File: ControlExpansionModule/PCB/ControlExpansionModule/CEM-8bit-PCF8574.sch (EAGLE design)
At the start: 0 parts

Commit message: Added component in the circuit
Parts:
- added C1, C2: (no value), rcl:C-EUC0805K
- added R1, R2, R3: (no value), rcl:R-EU_M1406
- added U1: PCF8574AT/3,512, PCF8574:PCF8574AT/3,512
- added X1: 43160-1204, con-molex:43160-1204
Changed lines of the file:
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@@
 <parts>
 <part name="FRAME1" library="frames" deviceset="A4L-LOC" device=""/>
+<part name="U1" library="PCF8574" deviceset="PCF8574AT/3,512" device=""/>
+<part name="R1" library="rcl" deviceset="R-EU_" device="M1406"/>
+<part name="R2" library="rcl" deviceset="R-EU_" device="M1406"/>
+<part name="R3" library="rcl" deviceset="R-EU_" device="M1406"/>
+<part name="X1" library="con-molex" deviceset="43160-*04" device="" technology="12"/>
+<part name="GND1" library="supply1" deviceset="GND" device=""/>
+<part name="P+1" library="supply1" deviceset="VCC" device=""/>
+<part name="C1" library="rcl" deviceset="C-EU" device="C0805K"/>
+<part name="C2" library="rcl" deviceset="C-EU" device="C0805K"/>
 </parts>
 <sheets>
@@
 <instances>
 <instance part="FRAME1" gate="G$1" x="0" y="0"/>
+<instance part="U1" gate="A" x="121.92" y="106.68"/>
+<instance part="R1" gate="G$1" x="71.12" y="121.92"/>
+<instance part="R2" gate="G$1" x="71.12" y="114.3"/>
+<instance part="R3" gate="G$1" x="71.12" y="106.68"/>
+<instance part="X1" gate="-1" x="25.4" y="119.38" rot="R180"/>
+<instance part="X1" gate="-2" x="25.4" y="121.92" rot="R180"/>
+<instance part="X1" gate="-3" x="25.4" y="124.46" rot="R180"/>
+<instance part="X1" gate="-4" x="25.4" y="127" rot="R180"/>
+<instance part="GND1" gate="1" x="33.02" y="109.22"/>
+<instance part="P+1" gate="VCC" x="35.56" y="139.7"/>
+<instance part="C1" gate="G$1" x="48.26" y="93.98"/>
+<instance part="C2" gate="G$1" x="48.26" y="76.2"/>
 </instances>
 <busses>

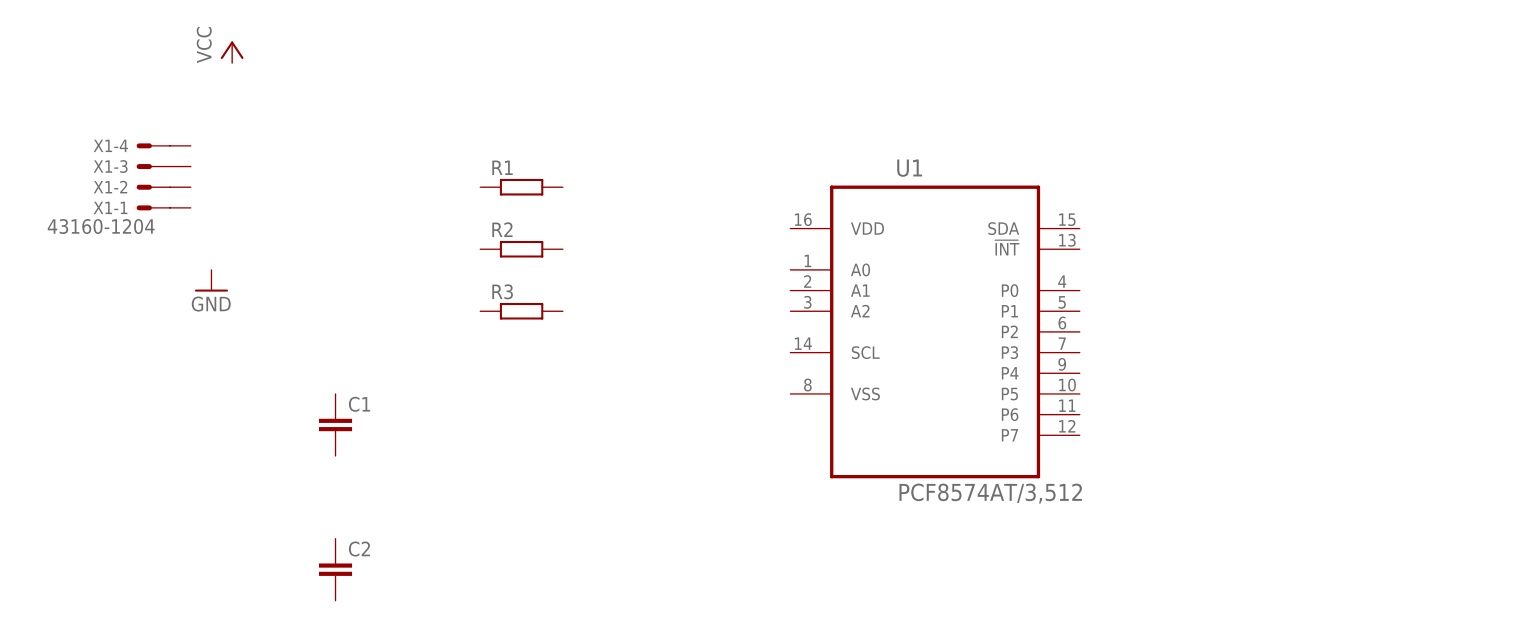
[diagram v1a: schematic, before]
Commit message: Wiring components in the Port expander circuit based on PCF8574
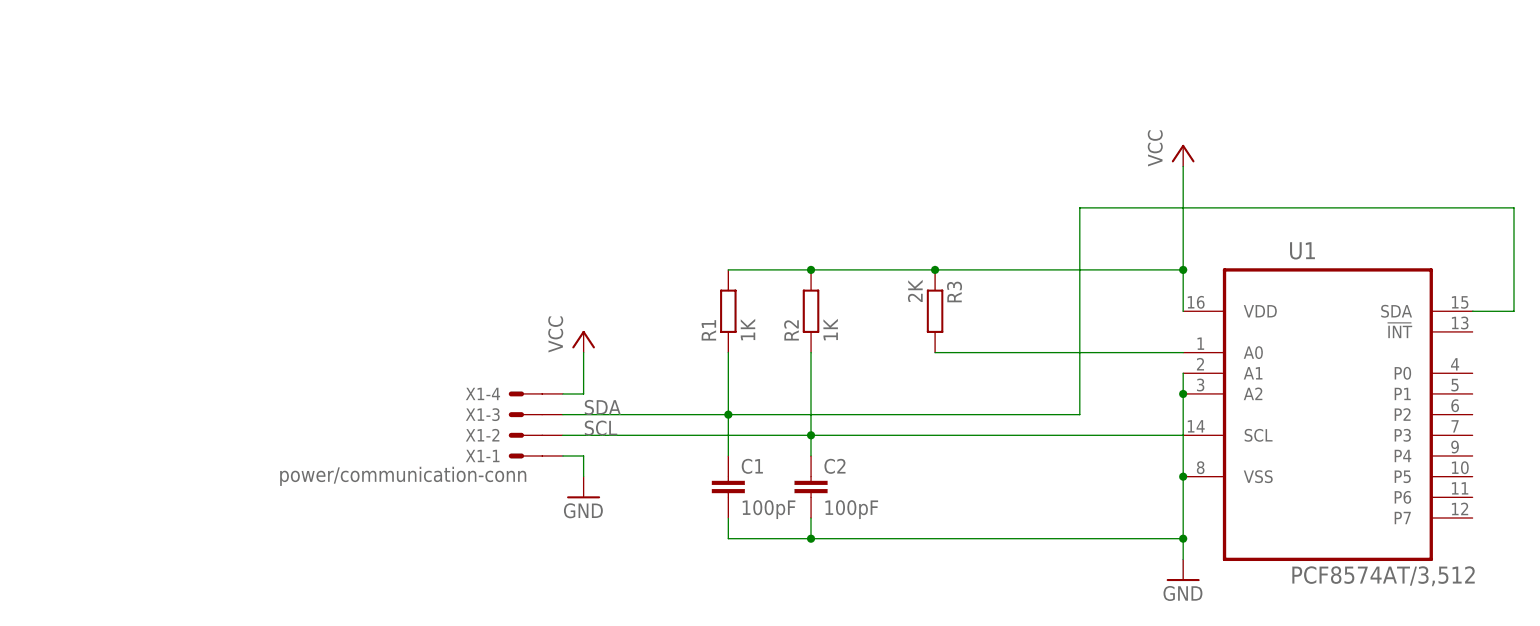
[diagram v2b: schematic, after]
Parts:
- C1, C2: value (none) -> 100pF
- R1, R2: value (none) -> 1K
- R3: value (none) -> 2K
- X1: value 43160-1204 -> power/communication-conn
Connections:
- new net GND: C1.2, C2.2, U1.A1, U1.A2, U1.VSS, X1-1.S@1
- new net N$1: R3.2, U1.A0
- new net SCL: C2.1, R2.1, U1.SCL, X1-2.S@1
- new net SDA: C1.1, R1.1, U1.SDA, X1-3.S@1
- new net VCC: R1.2, R2.2, R3.1, U1.VDD, X1-4.S@1
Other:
- moved on the sheet: C1, C2, R1, R2, R3, U1, X1-1, X1-2, X1-3, X1-4
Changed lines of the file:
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@@
 <part name="FRAME1" library="frames" deviceset="A4L-LOC" device=""/>
 <part name="U1" library="PCF8574" deviceset="PCF8574AT/3,512" device=""/>
-<part name="R1" library="rcl" deviceset="R-EU_" device="M1406"/>
-<part name="R2" library="rcl" deviceset="R-EU_" device="M1406"/>
-<part name="R3" library="rcl" deviceset="R-EU_" device="M1406"/>
-<part name="X1" library="con-molex" deviceset="43160-*04" device="" technology="12"/>
+<part name="R1" library="rcl" deviceset="R-EU_" device="M1406" value="1K"/>
+<part name="R2" library="rcl" deviceset="R-EU_" device="M1406" value="1K"/>
+<part name="R3" library="rcl" deviceset="R-EU_" device="M1406" value="2K"/>
+<part name="X1" library="con-molex" deviceset="43160-*04" device="" technology="12" value="power/communication-conn"/>
 <part name="GND1" library="supply1" deviceset="GND" device=""/>
 <part name="P+1" library="supply1" deviceset="VCC" device=""/>
-<part name="C1" library="rcl" deviceset="C-EU" device="C0805K"/>
-<part name="C2" library="rcl" deviceset="C-EU" device="C0805K"/>
+<part name="C1" library="rcl" deviceset="C-EU" device="C0805K" value="100pF"/>
+<part name="C2" library="rcl" deviceset="C-EU" device="C0805K" value="100pF"/>
+<part name="GND2" library="supply1" deviceset="GND" device=""/>
+<part name="P+2" library="supply1" deviceset="VCC" device=""/>
 </parts>
 <sheets>
@@
 <instances>
 <instance part="FRAME1" gate="G$1" x="0" y="0"/>
-<instance part="U1" gate="A" x="121.92" y="106.68"/>
-<instance part="R1" gate="G$1" x="71.12" y="121.92"/>
-<instance part="R2" gate="G$1" x="71.12" y="114.3"/>
-<instance part="R3" gate="G$1" x="71.12" y="106.68"/>
-<instance part="X1" gate="-1" x="25.4" y="119.38" rot="R180"/>
-<instance part="X1" gate="-2" x="25.4" y="121.92" rot="R180"/>
-<instance part="X1" gate="-3" x="25.4" y="124.46" rot="R180"/>
-<instance part="X1" gate="-4" x="25.4" y="127" rot="R180"/>
-<instance part="GND1" gate="1" x="33.02" y="109.22"/>
-<instance part="P+1" gate="VCC" x="35.56" y="139.7"/>
-<instance part="C1" gate="G$1" x="48.26" y="93.98"/>
-<instance part="C2" gate="G$1" x="48.26" y="76.2"/>
+<instance part="U1" gate="A" x="170.18" y="96.52"/>
+<instance part="R1" gate="G$1" x="96.52" y="106.68" rot="R90"/>
+<instance part="R2" gate="G$1" x="106.68" y="106.68" rot="R90"/>
+<instance part="R3" gate="G$1" x="121.92" y="106.68" rot="R270"/>
+<instance part="X1" gate="-1" x="71.12" y="88.9" rot="R180"/>
+<instance part="X1" gate="-2" x="71.12" y="91.44" rot="R180"/>
+<instance part="X1" gate="-3" x="71.12" y="93.98" rot="R180"/>
+<instance part="X1" gate="-4" x="71.12" y="96.52" rot="R180"/>
+<instance part="GND1" gate="1" x="78.74" y="83.82"/>
+<instance part="P+1" gate="VCC" x="152.4" y="127"/>
+<instance part="C1" gate="G$1" x="96.52" y="86.36"/>
+<instance part="C2" gate="G$1" x="106.68" y="86.36"/>
+<instance part="GND2" gate="1" x="152.4" y="73.66"/>
+<instance part="P+2" gate="VCC" x="78.74" y="104.14"/>
 </instances>
 <busses>
 </busses>
 <nets>
+<net name="VCC" class="0">
+<segment>
+<pinref part="P+1" gate="VCC" pin="VCC"/>
+<pinref part="U1" gate="A" pin="VDD"/>
+<wire x1="152.4" y1="124.46" x2="152.4" y2="111.76" width="0.1524" layer="91"/>
+<pinref part="R3" gate="G$1" pin="1"/>
+<wire x1="152.4" y1="111.76" x2="152.4" y2="106.68" width="0.1524" layer="91"/>
+<wire x1="121.92" y1="111.76" x2="152.4" y2="111.76" width="0.1524" layer="91"/>
+<pinref part="R1" gate="G$1" pin="2"/>
+<wire x1="96.52" y1="111.76" x2="106.68" y2="111.76" width="0.1524" layer="91"/>
+<pinref part="R2" gate="G$1" pin="2"/>
+<junction x="106.68" y="111.76"/>
+<wire x1="106.68" y1="111.76" x2="121.92" y2="111.76" width="0.1524" layer="91"/>
+<junction x="121.92" y="111.76"/>
+<junction x="152.4" y="111.76"/>
+</segment>
+<segment>
+<pinref part="X1" gate="-4" pin="S@1"/>
+<pinref part="P+2" gate="VCC" pin="VCC"/>
+<wire x1="76.2" y1="96.52" x2="78.74" y2="96.52" width="0.1524" layer="91"/>
+<wire x1="78.74" y1="96.52" x2="78.74" y2="101.6" width="0.1524" layer="91"/>
+</segment>
+</net>
+<net name="N$1" class="0">
+<segment>
+<pinref part="R3" gate="G$1" pin="2"/>
+<pinref part="U1" gate="A" pin="A0"/>
+<wire x1="121.92" y1="101.6" x2="152.4" y2="101.6" width="0.1524" layer="91"/>
+</segment>
+</net>
+<net name="SCL" class="0">
+<segment>
+<pinref part="R2" gate="G$1" pin="1"/>
+<pinref part="C2" gate="G$1" pin="1"/>
+<wire x1="106.68" y1="101.6" x2="106.68" y2="91.44" width="0.1524" layer="91"/>
+<pinref part="U1" gate="A" pin="SCL"/>
+<wire x1="106.68" y1="91.44" x2="106.68" y2="88.9" width="0.1524" layer="91"/>
+<wire x1="152.4" y1="91.44" x2="106.68" y2="91.44" width="0.1524" layer="91"/>
+<junction x="106.68" y="91.44"/>
+<wire x1="106.68" y1="91.44" x2="76.2" y2="91.44" width="0.1524" layer="91"/>
+<pinref part="X1" gate="-2" pin="S@1"/>
+<label x="78.74" y="91.44" size="1.778" layer="95"/>
+</segment>
+</net>
+<net name="SDA" class="0">
+<segment>
+<pinref part="R1" gate="G$1" pin="1"/>
+<pinref part="C1" gate="G$1" pin="1"/>
+<wire x1="96.52" y1="101.6" x2="96.52" y2="93.98" width="0.1524" layer="91"/>
+<pinref part="U1" gate="A" pin="SDA"/>
+<wire x1="96.52" y1="93.98" x2="96.52" y2="88.9" width="0.1524" layer="91"/>
+<wire x1="187.96" y1="106.68" x2="193.04" y2="106.68" width="0.1524" layer="91"/>
+<wire x1="193.04" y1="106.68" x2="193.04" y2="119.38" width="0.1524" layer="91"/>
+<wire x1="193.04" y1="119.38" x2="139.7" y2="119.38" width="0.1524" layer="91"/>
+<wire x1="139.7" y1="119.38" x2="139.7" y2="93.98" width="0.1524" layer="91"/>
+<wire x1="139.7" y1="93.98" x2="96.52" y2="93.98" width="0.1524" layer="91"/>
+<junction x="96.52" y="93.98"/>
+<wire x1="96.52" y1="93.98" x2="76.2" y2="93.98" width="0.1524" layer="91"/>
+<pinref part="X1" gate="-3" pin="S@1"/>
+<label x="78.74" y="93.98" size="1.778" layer="95"/>
+</segment>
+</net>
+<net name="GND" class="0">
+<segment>
+<pinref part="U1" gate="A" pin="VSS"/>
+<pinref part="GND2" gate="1" pin="GND"/>
+<wire x1="152.4" y1="86.36" x2="152.4" y2="78.74" width="0.1524" layer="91"/>
+<pinref part="C1" gate="G$1" pin="2"/>
+<wire x1="152.4" y1="78.74" x2="152.4" y2="76.2" width="0.1524" layer="91"/>
+<wire x1="96.52" y1="81.28" x2="96.52" y2="78.74" width="0.1524" layer="91"/>
+<wire x1="96.52" y1="78.74" x2="106.68" y2="78.74" width="0.1524" layer="91"/>
+<pinref part="C2" gate="G$1" pin="2"/>
+<wire x1="106.68" y1="78.74" x2="152.4" y2="78.74" width="0.1524" layer="91"/>
+<wire x1="106.68" y1="81.28" x2="106.68" y2="78.74" width="0.1524" layer="91"/>
+<junction x="106.68" y="78.74"/>
+<junction x="152.4" y="78.74"/>
+<pinref part="U1" gate="A" pin="A1"/>
+<pinref part="U1" gate="A" pin="A2"/>
+<wire x1="152.4" y1="99.06" x2="152.4" y2="96.52" width="0.1524" layer="91"/>
+<wire x1="152.4" y1="96.52" x2="152.4" y2="86.36" width="0.1524" layer="91"/>
+<junction x="152.4" y="96.52"/>
+<junction x="152.4" y="86.36"/>
+</segment>
+<segment>
+<pinref part="X1" gate="-1" pin="S@1"/>
+<pinref part="GND1" gate="1" pin="GND"/>
+<wire x1="76.2" y1="88.9" x2="78.74" y2="88.9" width="0.1524" layer="91"/>
+<wire x1="78.74" y1="88.9" x2="78.74" y2="86.36" width="0.1524" layer="91"/>
+</segment>
+</net>
 </nets>
 </sheet>
